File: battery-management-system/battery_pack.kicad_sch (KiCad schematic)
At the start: 26 parts, among them J1 CELL4_PLUS, J2 CELL4_MINUS, J3 CELL3_MINUS, J4 CELL2_MINUS, J5 CELL1_MINUS, J6 VBAT+, J7 VBAT+_CHARGE, J8 VBAT-, Q1 DMN3404L, Q2 TJ40S04M3L, Q3 TJ40S04M3L, Q4 DMN3404L, Q5 DMN3404L

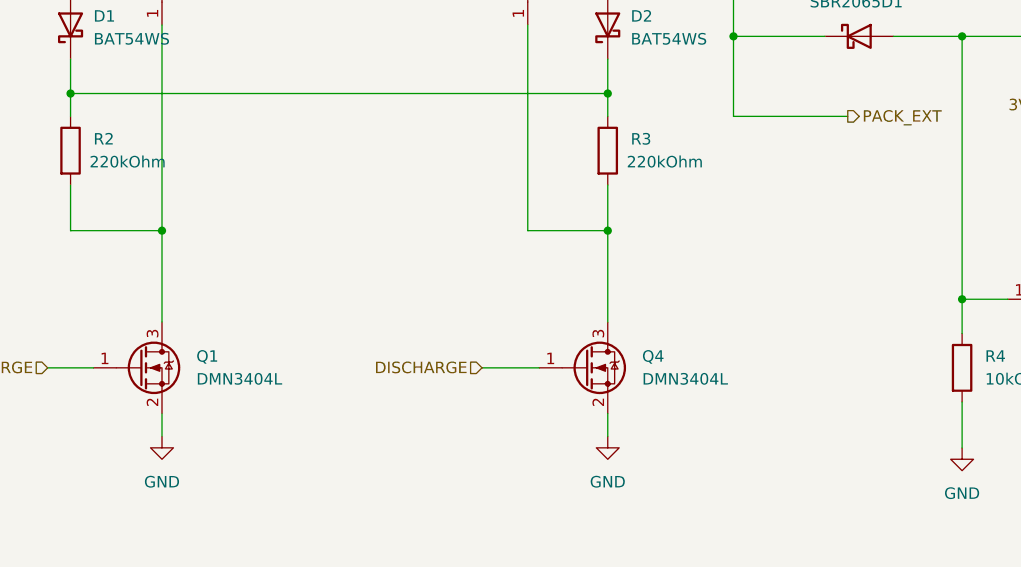
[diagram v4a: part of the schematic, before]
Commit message: add overrides for charge and discharge
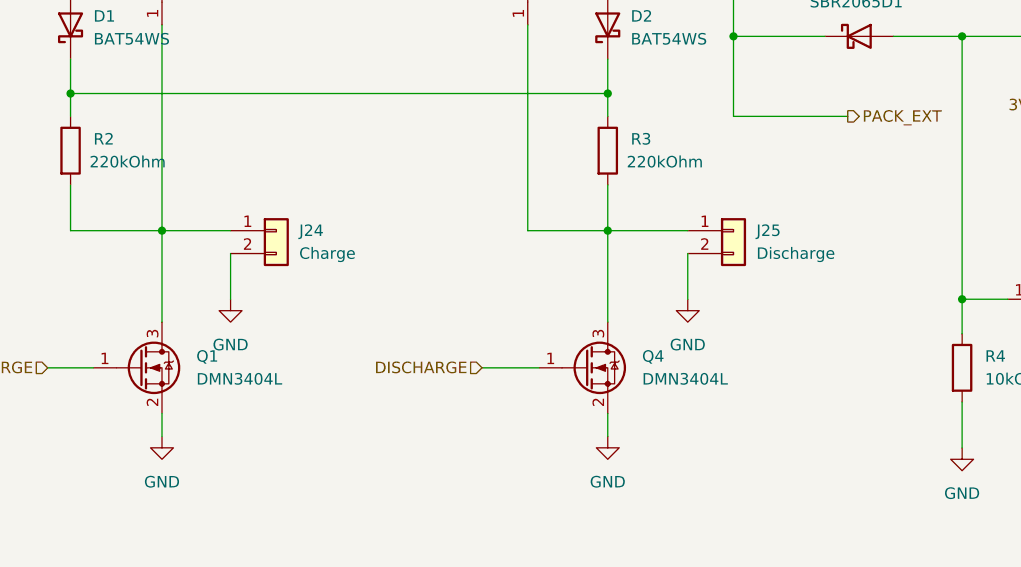
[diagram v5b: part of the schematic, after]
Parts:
- added J24: Charge, benediktibk:PinHeader_1x02_P2.54mm_Vertical, symbol benediktibk:Conn_01x02
- added J25: Discharge, benediktibk:PinHeader_1x02_P2.54mm_Vertical, symbol benediktibk:Conn_01x02
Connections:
- net GND: now also J24.2 (Pin_2), J25.2 (Pin_2)
- net at Q1.3 (D), Q2.1 (G), R2.2: now also J24.1 (Pin_1)
- net at Q3.1 (G), Q4.3 (D), R3.2: now also J25.1 (Pin_1)
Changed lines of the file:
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@@
+    (stroke (width 0) (type default))
+  )
+  (wire (pts (xy 144.78 74.93) (xy 153.67 74.93))
     (stroke (width 0) (type default))
   )
@@
     (stroke (width 0) (type default))
   )
+  (wire (pts (xy 102.87 77.47) (xy 102.87 82.55))
+    (stroke (width 0) (type default))
+  )
   (wire (pts (xy 226.06 86.36) (xy 218.44 86.36))
     (stroke (width 0) (type default))
@@
     (stroke (width 0) (type default))
   )
+  (wire (pts (xy 153.67 77.47) (xy 153.67 82.55))
+    (stroke (width 0) (type default))
+  )
   (wire (pts (xy 158.75 53.34) (xy 158.75 44.45))
     (stroke (width 0) (type default))
@@
   )
   (wire (pts (xy 240.03 44.45) (xy 262.89 44.45))
+    (stroke (width 0) (type default))
+  )
+  (wire (pts (xy 95.25 74.93) (xy 102.87 74.93))
     (stroke (width 0) (type default))
   )
@@
     )
   )
+  (symbol (lib_id "power:GND") (at 153.67 82.55 0) (unit 1)
+    (in_bom yes) (on_board yes) (dnp no) (fields_autoplaced)
+    (property "Reference" "#PWR085" (at 153.67 88.9 0)
+      (effects (font (size 1.27 1.27)) hide)
+    )
+    (property "Value" "GND" (at 153.67 87.63 0)
+      (effects (font (size 1.27 1.27)))
+    )
+    (property "Footprint" "" (at 153.67 82.55 0)
+      (effects (font (size 1.27 1.27)) hide)
+    )
+    (property "Datasheet" "" (at 153.67 82.55 0)
+      (effects (font (size 1.27 1.27)) hide)
+    )
+    (pin "1")
+    (instances
+      (project "battery-management-system"
+        (path "/5272f0ff-3069-41a9-bca2-80beede8b4b2/31b87c35-c096-4dc0-8978-834bec283b57"
+          (reference "#PWR085") (unit 1)
+        )
+      )
+    )
+  )
   (symbol (lib_id "benediktibk:SBR2065D1") (at 226.06 69.85 90) (mirror x) (unit 1)
     (in_bom yes) (on_board yes) (dnp no) (fields_autoplaced)
@@
         (path "/5272f0ff-3069-41a9-bca2-80beede8b4b2/31b87c35-c096-4dc0-8978-834bec283b57"
           (reference "F2") (unit 1)
+        )
+      )
+    )
+  )
+  (symbol (lib_id "benediktibk:Conn_01x02") (at 106.68 73.66 0) (unit 1)
+    (in_bom yes) (on_board yes) (dnp no) (fields_autoplaced)
+    (property "Reference" "J24" (at 110.49 74.93 0)
+      (effects (font (size 1.27 1.27)) (justify left))
+    )
+    (property "Value" "Charge" (at 110.49 77.47 0)
+      (effects (font (size 1.27 1.27)) (justify left))
+    )
+    (property "Footprint" "benediktibk:PinHeader_1x02_P2.54mm_Vertical" (at 106.68 73.66 0)
+      (effects (font (size 1.27 1.27)) hide)
+    )
+    (property "Datasheet" "~" (at 106.68 73.66 0)
+      (effects (font (size 1.27 1.27)) hide)
+    )
+    (property "RS order number" "251-8086" (at 106.68 73.66 0)
+      (effects (font (size 1.27 1.27)) hide)
+    )
+    (pin "1")
+    (pin "2")
+    (instances
+      (project "battery-management-system"
+        (path "/5272f0ff-3069-41a9-bca2-80beede8b4b2/31b87c35-c096-4dc0-8978-834bec283b57"
+          (reference "J24") (unit 1)
         )
       )
@@
     )
   )
+  (symbol (lib_id "benediktibk:Conn_01x02") (at 157.48 73.66 0) (unit 1)
+    (in_bom yes) (on_board yes) (dnp no) (fields_autoplaced)
+    (property "Reference" "J25" (at 161.29 74.93 0)
+      (effects (font (size 1.27 1.27)) (justify left))
+    )
+    (property "Value" "Discharge" (at 161.29 77.47 0)
+      (effects (font (size 1.27 1.27)) (justify left))
+    )
+    (property "Footprint" "benediktibk:PinHeader_1x02_P2.54mm_Vertical" (at 157.48 73.66 0)
+      (effects (font (size 1.27 1.27)) hide)
+    )
+    (property "Datasheet" "~" (at 157.48 73.66 0)
+      (effects (font (size 1.27 1.27)) hide)
+    )
+    (property "RS order number" "251-8086" (at 157.48 73.66 0)
+      (effects (font (size 1.27 1.27)) hide)
+    )
+    (pin "1")
+    (pin "2")
+    (instances
+      (project "battery-management-system"
+        (path "/5272f0ff-3069-41a9-bca2-80beede8b4b2/31b87c35-c096-4dc0-8978-834bec283b57"
+          (reference "J25") (unit 1)
+        )
+      )
+    )
+  )
   (symbol (lib_id "benediktibk:BAT54WS") (at 144.78 52.07 90) (unit 1)
     (in_bom yes) (on_board yes) (dnp no) (fields_autoplaced)
@@
         )
       )
+    )
+  )
+  (symbol (lib_id "power:GND") (at 102.87 82.55 0) (unit 1)
+    (in_bom yes) (on_board yes) (dnp no) (fields_autoplaced)
+    (property "Reference" "#PWR084" (at 102.87 88.9 0)
+      (effects (font (size 1.27 1.27)) hide)
+    )
+    (property "Value" "GND" (at 102.87 87.63 0)
+      (effects (font (size 1.27 1.27)))
+    )
+    (property "Footprint" "" (at 102.87 82.55 0)
+      (effects (font (size 1.27 1.27)) hide)
+    )
+    (property "Datasheet" "" (at 102.87 82.55 0)
+      (effects (font (size 1.27 1.27)) hide)
+    )
+    (pin "1")
+    (instances
+      (project "battery-management-system"
+        (path "/5272f0ff-3069-41a9-bca2-80beede8b4b2/31b87c35-c096-4dc0-8978-834bec283b57"
+          (reference "#PWR084") (unit 1)
+        )
+      )
